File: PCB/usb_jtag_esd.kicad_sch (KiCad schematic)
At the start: 4 parts, among them U10 TPAZ1043-04F, U11 TPAZ1043-04F, U12 TPAZ1043-04F, U9 TPAZ1043-04F

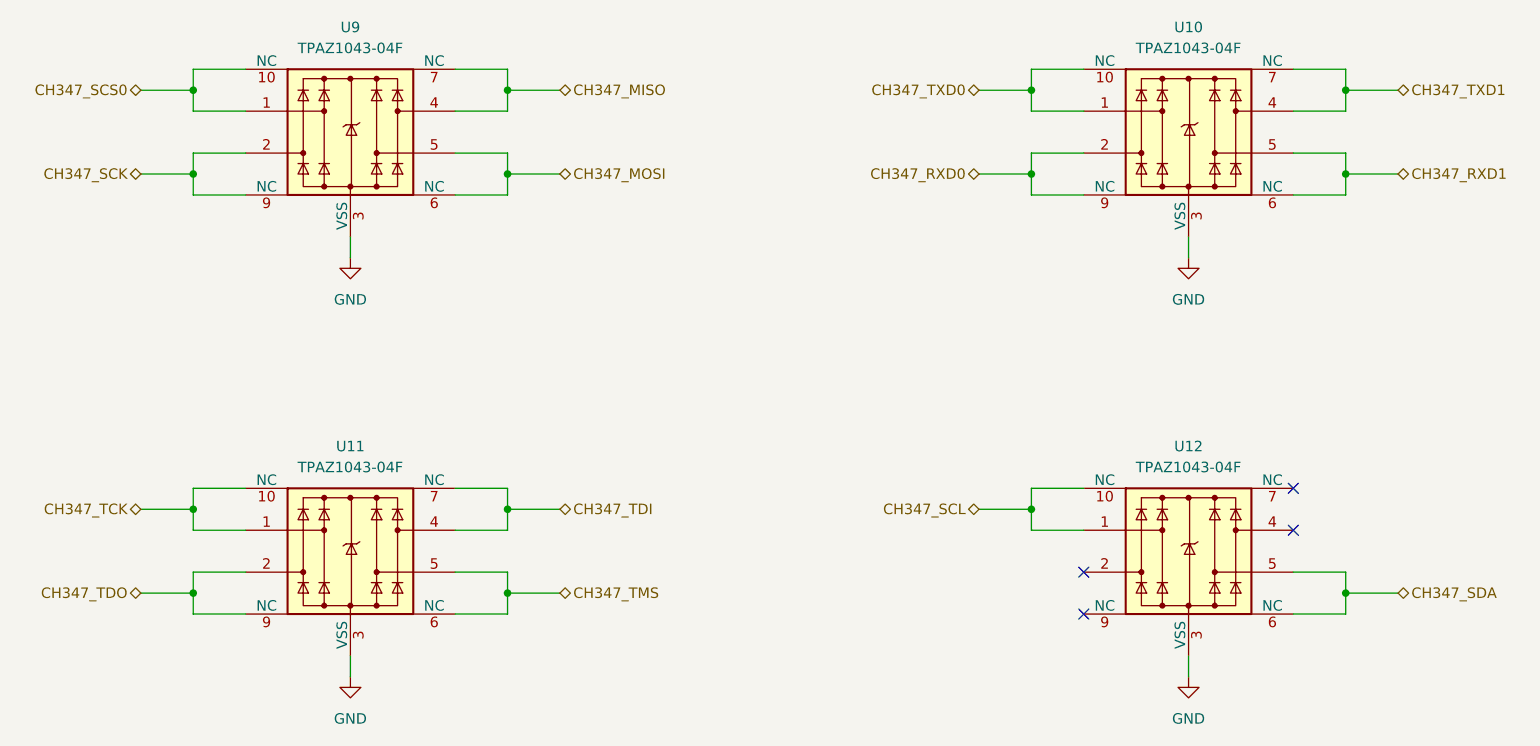
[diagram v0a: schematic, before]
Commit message: Improve the ESD protection
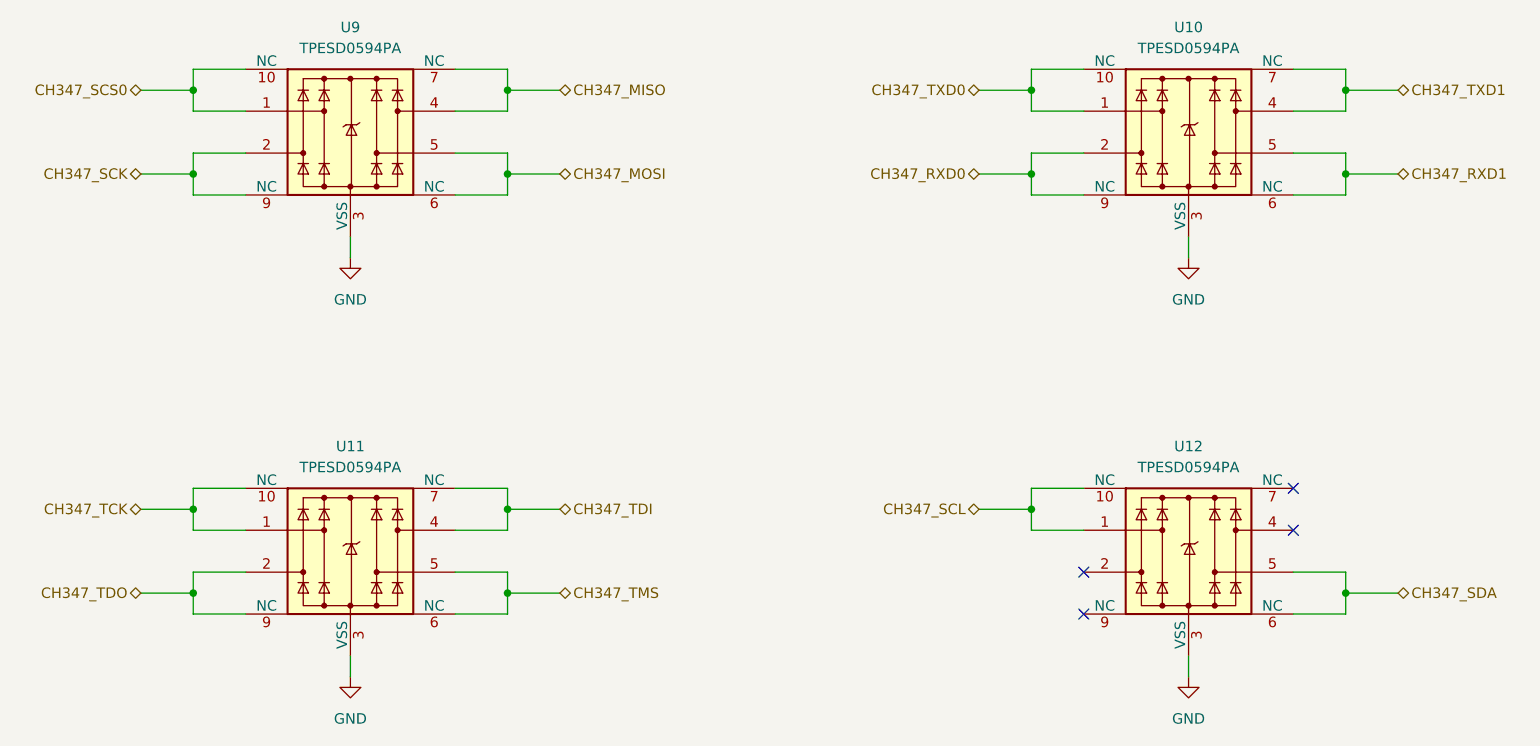
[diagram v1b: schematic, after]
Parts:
- U10, U11, U12, U9: value TPAZ1043-04F -> TPESD0594PA; LCSC C2827673 -> C42436622; Part_number TPAZ1043-04F -> TPESD0594PA
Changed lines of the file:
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@@
 		(dnp no)
 		(fields_autoplaced yes)
-		(property "Reference" "#PWR045"
+		(property "Reference" "#PWR047"
 			(at 203.2 91.44 0)
 			(effects
@@
 			(project "clavier"
 				(path "/6362c6e0-59ef-40d3-b6e0-7e9dfe7b9b20/363c396c-f7c0-4911-9972-4574f7737631/43d27599-c6f7-424d-a87e-55a1d50df649"
-					(reference "#PWR045")
+					(reference "#PWR047")
 					(unit 1)
 				)
@@
 			)
 		)
-		(property "Value" "TPAZ1043-04F"
+		(property "Value" "TPESD0594PA"
 			(at 203.2 110.49 0)
 			(effects
@@
 			)
 		)
-		(property "Datasheet" "https://www.lcsc.com/datasheet/lcsc_datasheet_2411121100_TECH-PUBLIC-TPAZ1043-04F_C2827673.pdf"
+		(property "Datasheet" "https://www.lcsc.com/datasheet/lcsc_datasheet_2501161435_TECH-PUBLIC-TPESD0594PA_C42436622.pdf"
 			(at 203.2 120.65 0)
 			(effects
@@
 			)
 		)
-		(property "LCSC" "C2827673"
+		(property "LCSC" "C42436622"
 			(at 203.2 120.65 0)
 			(effects
@@
 			)
 		)
-		(property "Part_number" "TPAZ1043-04F"
+		(property "Part_number" "TPESD0594PA"
 			(at 203.2 120.65 0)
 			(effects
@@
 			)
 		)
-		(property "Value" "TPAZ1043-04F"
+		(property "Value" "TPESD0594PA"
 			(at 101.6 59.69 0)
 			(effects
@@
 			)
 		)
-		(property "Datasheet" "https://www.lcsc.com/datasheet/lcsc_datasheet_2411121100_TECH-PUBLIC-TPAZ1043-04F_C2827673.pdf"
+		(property "Datasheet" "https://www.lcsc.com/datasheet/lcsc_datasheet_2501161435_TECH-PUBLIC-TPESD0594PA_C42436622.pdf"
 			(at 101.6 69.85 0)
 			(effects
@@
 			)
 		)
-		(property "LCSC" "C2827673"
+		(property "LCSC" "C42436622"
 			(at 101.6 69.85 0)
 			(effects
@@
 			)
 		)
-		(property "Part_number" "TPAZ1043-04F"
+		(property "Part_number" "TPESD0594PA"
 			(at 101.6 69.85 0)
 			(effects
@@
 			)
 		)
-		(property "Value" "TPAZ1043-04F"
+		(property "Value" "TPESD0594PA"
 			(at 203.2 59.69 0)
 			(effects
@@
 			)
 		)
-		(property "Datasheet" "https://www.lcsc.com/datasheet/lcsc_datasheet_2411121100_TECH-PUBLIC-TPAZ1043-04F_C2827673.pdf"
+		(property "Datasheet" "https://www.lcsc.com/datasheet/lcsc_datasheet_2501161435_TECH-PUBLIC-TPESD0594PA_C42436622.pdf"
 			(at 203.2 69.85 0)
 			(effects
@@
 			)
 		)
-		(property "LCSC" "C2827673"
+		(property "LCSC" "C42436622"
 			(at 203.2 69.85 0)
 			(effects
@@
 			)
 		)
-		(property "Part_number" "TPAZ1043-04F"
+		(property "Part_number" "TPESD0594PA"
 			(at 203.2 69.85 0)
 			(effects
@@
 			)
 		)
-		(property "Value" "TPAZ1043-04F"
+		(property "Value" "TPESD0594PA"
 			(at 101.6 110.49 0)
 			(effects
@@
 			)
 		)
-		(property "Datasheet" "https://www.lcsc.com/datasheet/lcsc_datasheet_2411121100_TECH-PUBLIC-TPAZ1043-04F_C2827673.pdf"
+		(property "Datasheet" "https://www.lcsc.com/datasheet/lcsc_datasheet_2501161435_TECH-PUBLIC-TPESD0594PA_C42436622.pdf"
 			(at 101.6 120.65 0)
 			(effects
@@
 			)
 		)
-		(property "LCSC" "C2827673"
+		(property "LCSC" "C42436622"
 			(at 101.6 120.65 0)
 			(effects
@@
 			)
 		)
-		(property "Part_number" "TPAZ1043-04F"
+		(property "Part_number" "TPESD0594PA"
 			(at 101.6 120.65 0)
 			(effects
@@
 		(dnp no)
 		(fields_autoplaced yes)
-		(property "Reference" "#PWR046"
+		(property "Reference" "#PWR048"
 			(at 101.6 142.24 0)
 			(effects
@@
 			(project "clavier"
 				(path "/6362c6e0-59ef-40d3-b6e0-7e9dfe7b9b20/363c396c-f7c0-4911-9972-4574f7737631/43d27599-c6f7-424d-a87e-55a1d50df649"
-					(reference "#PWR046")
+					(reference "#PWR048")
 					(unit 1)
 				)
@@
 		(dnp no)
 		(fields_autoplaced yes)
-		(property "Reference" "#PWR044"
+		(property "Reference" "#PWR046"
 			(at 101.6 91.44 0)
 			(effects
@@
 			(project "clavier"
 				(path "/6362c6e0-59ef-40d3-b6e0-7e9dfe7b9b20/363c396c-f7c0-4911-9972-4574f7737631/43d27599-c6f7-424d-a87e-55a1d50df649"
-					(reference "#PWR044")
+					(reference "#PWR046")
 					(unit 1)
 				)
@@
 		(dnp no)
 		(fields_autoplaced yes)
-		(property "Reference" "#PWR047"
+		(property "Reference" "#PWR049"
 			(at 203.2 142.24 0)
 			(effects
@@
 			(project "clavier"
 				(path "/6362c6e0-59ef-40d3-b6e0-7e9dfe7b9b20/363c396c-f7c0-4911-9972-4574f7737631/43d27599-c6f7-424d-a87e-55a1d50df649"
-					(reference "#PWR047")
-					(unit 1)
-				)
+					(reference "#PWR049")
+					(unit 1)
+				)

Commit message: Complete the PCB routing
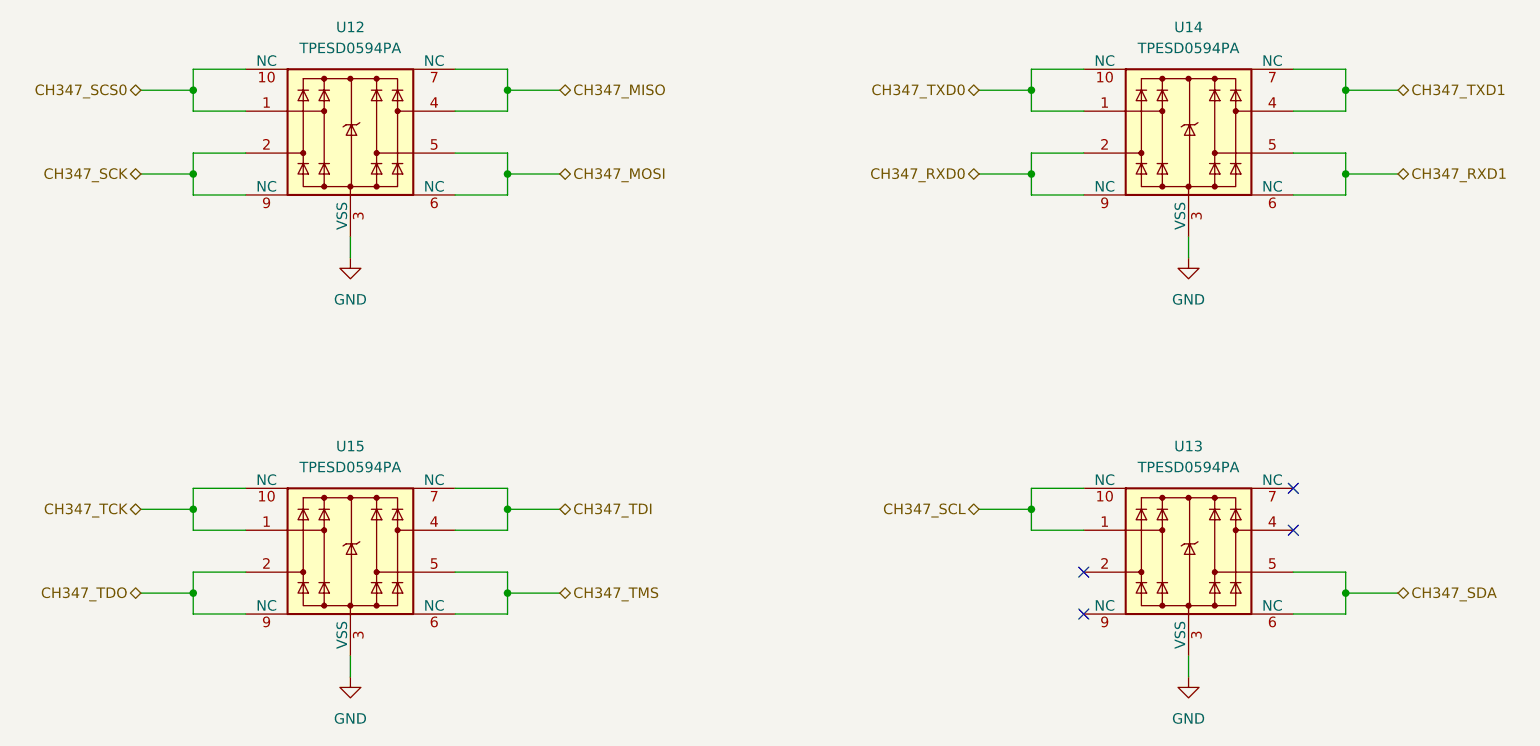
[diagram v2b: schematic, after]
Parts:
- renumbered U9 to U12, U12 to U13, U10 to U14, U11 to U15
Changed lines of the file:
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@@
 	(title_block
 		(title "Clavier - 5-in-1 USB ESD protection")
-		(date "2025-06-21")
+		(date "2025-06-22")
 		(rev "1.0")
 		(company "Copyright (c) 2025 L. Sartory")
@@
 		(dnp no)
 		(fields_autoplaced yes)
-		(property "Reference" "U12"
+		(property "Reference" "U13"
 			(at 203.2 107.95 0)
 			(effects
@@
 			(project "clavier"
 				(path "/6362c6e0-59ef-40d3-b6e0-7e9dfe7b9b20/363c396c-f7c0-4911-9972-4574f7737631/43d27599-c6f7-424d-a87e-55a1d50df649"
-					(reference "U12")
+					(reference "U13")
 					(unit 1)
 				)
@@
 		(dnp no)
 		(fields_autoplaced yes)
-		(property "Reference" "U9"
+		(property "Reference" "U12"
 			(at 101.6 57.15 0)
 			(effects
@@
 			(project "clavier"
 				(path "/6362c6e0-59ef-40d3-b6e0-7e9dfe7b9b20/363c396c-f7c0-4911-9972-4574f7737631/43d27599-c6f7-424d-a87e-55a1d50df649"
-					(reference "U9")
+					(reference "U12")
 					(unit 1)
 				)
@@
 		(dnp no)
 		(fields_autoplaced yes)
-		(property "Reference" "U10"
+		(property "Reference" "U14"
 			(at 203.2 57.15 0)
 			(effects
@@
 			(project "clavier"
 				(path "/6362c6e0-59ef-40d3-b6e0-7e9dfe7b9b20/363c396c-f7c0-4911-9972-4574f7737631/43d27599-c6f7-424d-a87e-55a1d50df649"
-					(reference "U10")
+					(reference "U14")
 					(unit 1)
 				)
@@
 		(dnp no)
 		(fields_autoplaced yes)
-		(property "Reference" "U11"
+		(property "Reference" "U15"
 			(at 101.6 107.95 0)
 			(effects
@@
 			(project "clavier"
 				(path "/6362c6e0-59ef-40d3-b6e0-7e9dfe7b9b20/363c396c-f7c0-4911-9972-4574f7737631/43d27599-c6f7-424d-a87e-55a1d50df649"
-					(reference "U11")
+					(reference "U15")
 					(unit 1)
 				)
